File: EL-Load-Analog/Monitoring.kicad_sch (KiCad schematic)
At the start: 65 parts, among them J301 VSense, Q301 2N7002, Q302 BSS138, U301 LM833, U302 LM833, U303 OPA189/MCP6V51/LTC2050HV, U304 OPA189/MCP6V51/LTC2050HV, U305 74HCT02, U306 LM393

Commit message: Major Analog PCB update DAC/ADC + connectors included, fan IC removed
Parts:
- removed J301: VSense, Connector_PinHeader_2.54mm:PinHeader_1x02_P2.54mm_Vertical, symbol Connector:Conn_01x02_Pin
- removed JP301, JP302: Jumper_2_Open, Connector_PinHeader_2.54mm:PinHeader_1x02_P2.54mm_Vertical, symbol Jumper:Jumper_2_Open
- removed JP303, JP304: Jumper_3_Open, Connector_PinHeader_2.54mm:PinHeader_1x03_P2.54mm_Vertical, symbol Jumper:Jumper_3_Open
- removed Q302: BSS138, Package_TO_SOT_SMD:SOT-23, symbol Transistor_FET:BSS138
- removed R326, R327, R328: 10k, Resistor_SMD:R_0805_2012Metric_Pad1.20x1.40mm_HandSolder, symbol Device:R_Small
- removed R329: 20k, Resistor_SMD:R_0805_2012Metric_Pad1.20x1.40mm_HandSolder, symbol Device:R_Small
- added D2, D3: 1N4148, Diode_SMD:D_MiniMELF, symbol Diode:1N4148
- added J6: Conn_02x03_Counter_Clockwise, Connector_PinHeader_2.54mm:PinHeader_2x03_P2.54mm_Vertical_SMD, symbol Connector_Generic:Conn_02x03_Counter_Clockwise
- added K2: EE2-5TNU, Relay_SMD:Relay_DPDT_Kemet_EE2_NU_DoubleCoil, symbol Relay:EE2-5TNU
- added Q1, Q2: 2N7002, Package_TO_SOT_SMD:SOT-23, symbol Transistor_FET:2N7002
- added R1, R16, R18, R19, R20: 100k, Resistor_SMD:R_0805_2012Metric, symbol Device:R_Small
- added U8, U9: VO1400AEFTR, Package_SO:SO-4_4.4x4.3mm_P2.54mm, symbol Relay_SolidState:ASSR-1218
- C1, C2, C301, C302, C303, C304, C305, C306, C307, C308, C309, C310, C311, C312, C313, C314, C315, C316: footprint Capacitor_SMD:C_0805_2012Metric_Pad1.18x1.45mm_HandSolder -> Capacitor_SMD:C_0805_2012Metric
- D301, D302: footprint Diode_SMD:D_MiniMELF_Handsoldering -> Diode_SMD:D_MiniMELF
- JP305: footprint Connector_PinHeader_2.54mm:PinHeader_1x02_P2.54mm_Vertical -> Jumper:SolderJumper-2_P1.3mm_Bridged_RoundedPad1.0x1.5mm
- JP306: footprint Connector_PinHeader_2.54mm:PinHeader_1x02_P2.54mm_Vertical -> Jumper:SolderJumper-2_P1.3mm_Bridged2Bar_RoundedPad1.0x1.5mm
- R301, R302, R303, R304, R305, R306, R307, R308, R309, R310, R311, R312, R313, R314, R315, R316, R317, R318, R319, R320, R321, R322, R323, R324, R325, R330: footprint Resistor_SMD:R_0805_2012Metric_Pad1.20x1.40mm_HandSolder -> Resistor_SMD:R_0805_2012Metric
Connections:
- net -GCOM is gone; now on net GND: U302.5 (+)
- net 4GCOM is gone; now on net GCOM: R315.2
- net +5V: now also D2.1 (K), D3.1 (K), J6.5 (Pin_5), K2.1, K2.6
- net GCOM: now also J6.4 (Pin_4)
- net GND: now also J6.6 (Pin_6), Q1.2 (S), Q2.2 (S), R1.1, R16.1, R20.1, U8.2, U9.2
- net Imon: now also J6.2 (Pin_2)
- net LoadMinMon: now also K2.10
- net LoadPlusMon: now also K2.3
- net LoopImon: now also J6.1 (Pin_1)
- net ~{VonLatch}: now also U305.12
- net ~{Von}: now also Q301.1 (G), U305.4
- net at R312.1, R314.2: now also U9.3
- net at R306.1, R308.2, U303.4 (-): now also U9.4
- net at R316.1, R319.2, U304.4 (-): now also J6.3 (Pin_3)
- net at R305.1, R307.1, U303.3 (+): now also U8.3
- net at R317.2: now also K2.4
- net at R311.2, R313.1: now also U8.4
- net at C310.2, R321.2, U306.3 (+): now also R1.2
- net at R318.1: now also K2.9
- net CCsetOut renamed Iset
- net VonsetComp renamed Vonset
- new net: D3.2 (A), K2.7, Q2.3 (D)
- new net: R19.1, U9.1
- new net: D2.2 (A), K2.12, Q1.3 (D)
- new net: R18.1, U8.1
- new net LoadMinSense: K2.8
- new net LoadPlusSense: K2.5
- new net VoltRangeLow: R18.2, R19.2
- new net VsenseClear: Q2.1 (G), R20.2
- new net VsenseSet: Q1.1 (G), R16.2
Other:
- note added: "For scaling Von"
- note added: "For testing current ranges"
- note added: "Sense selection"
- note added: "TODO: Add protection diodes"
- note added: "TODO: Check this, was -GCOM (-50mV)"
- note added: "Von = VonSet * 34 * 15/16 - 1.6"
- note added: "high(80V)/low(9V) range"
- note removed: "Manual high(80V)/low(9V) range"
- note removed: "Manual sense selection"
- moved on the sheet: C307, C308, R321

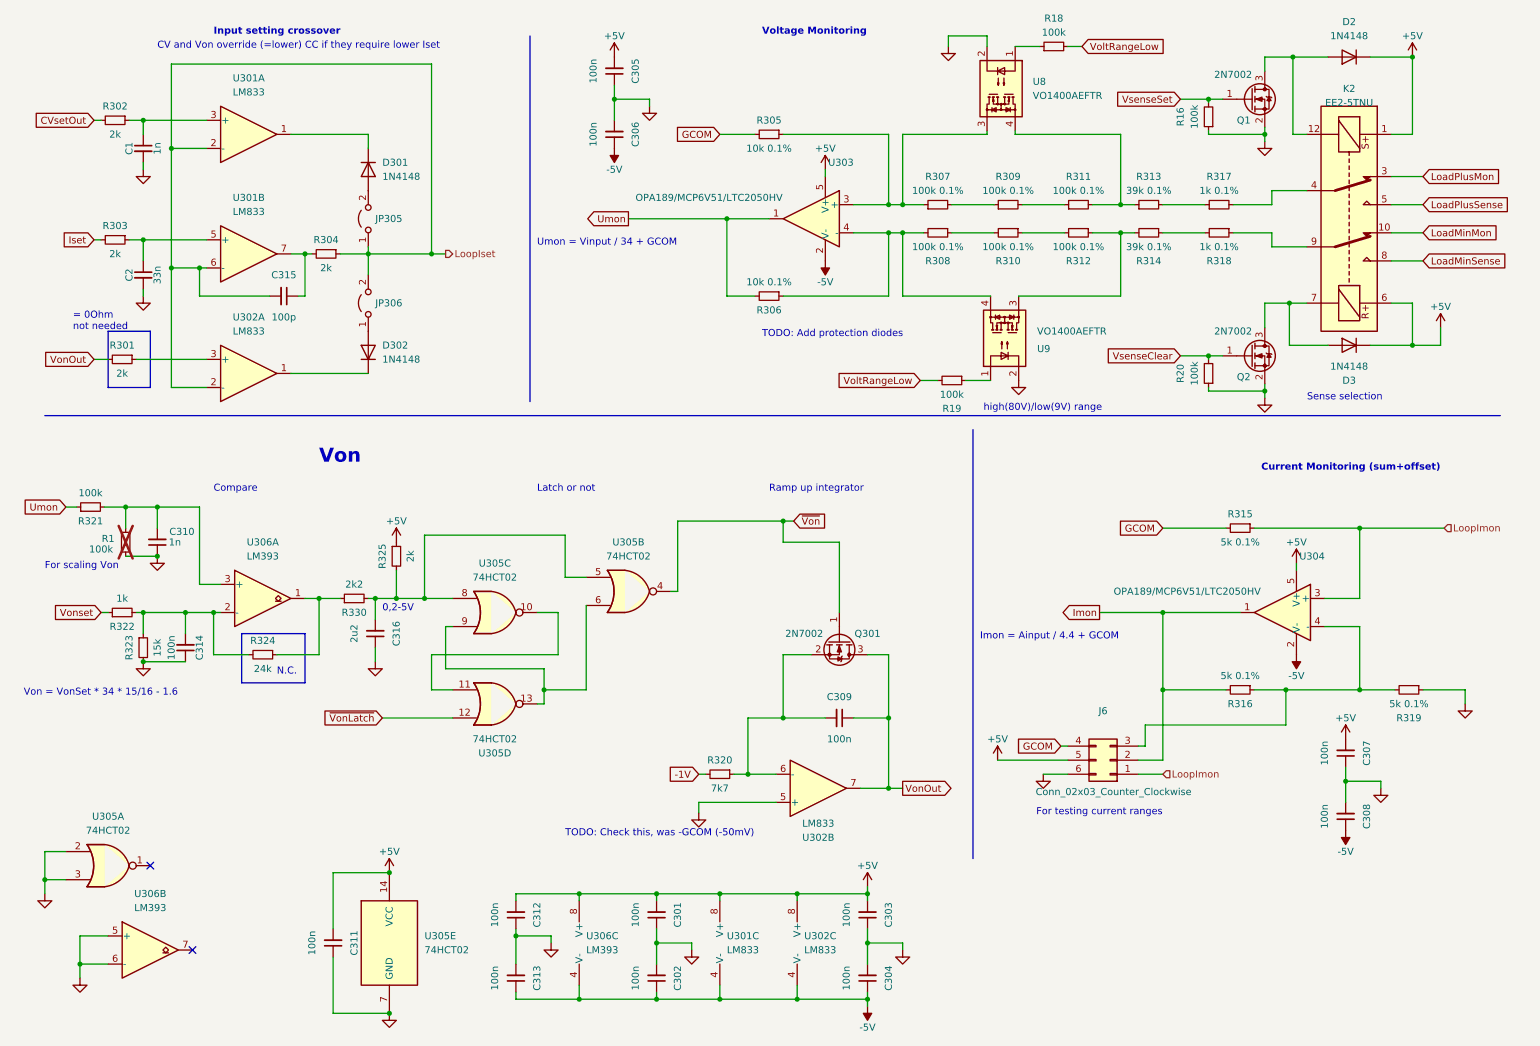
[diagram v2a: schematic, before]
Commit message: Added SenseError detection (including ocmponents), added clearances, fixed few BOM items.
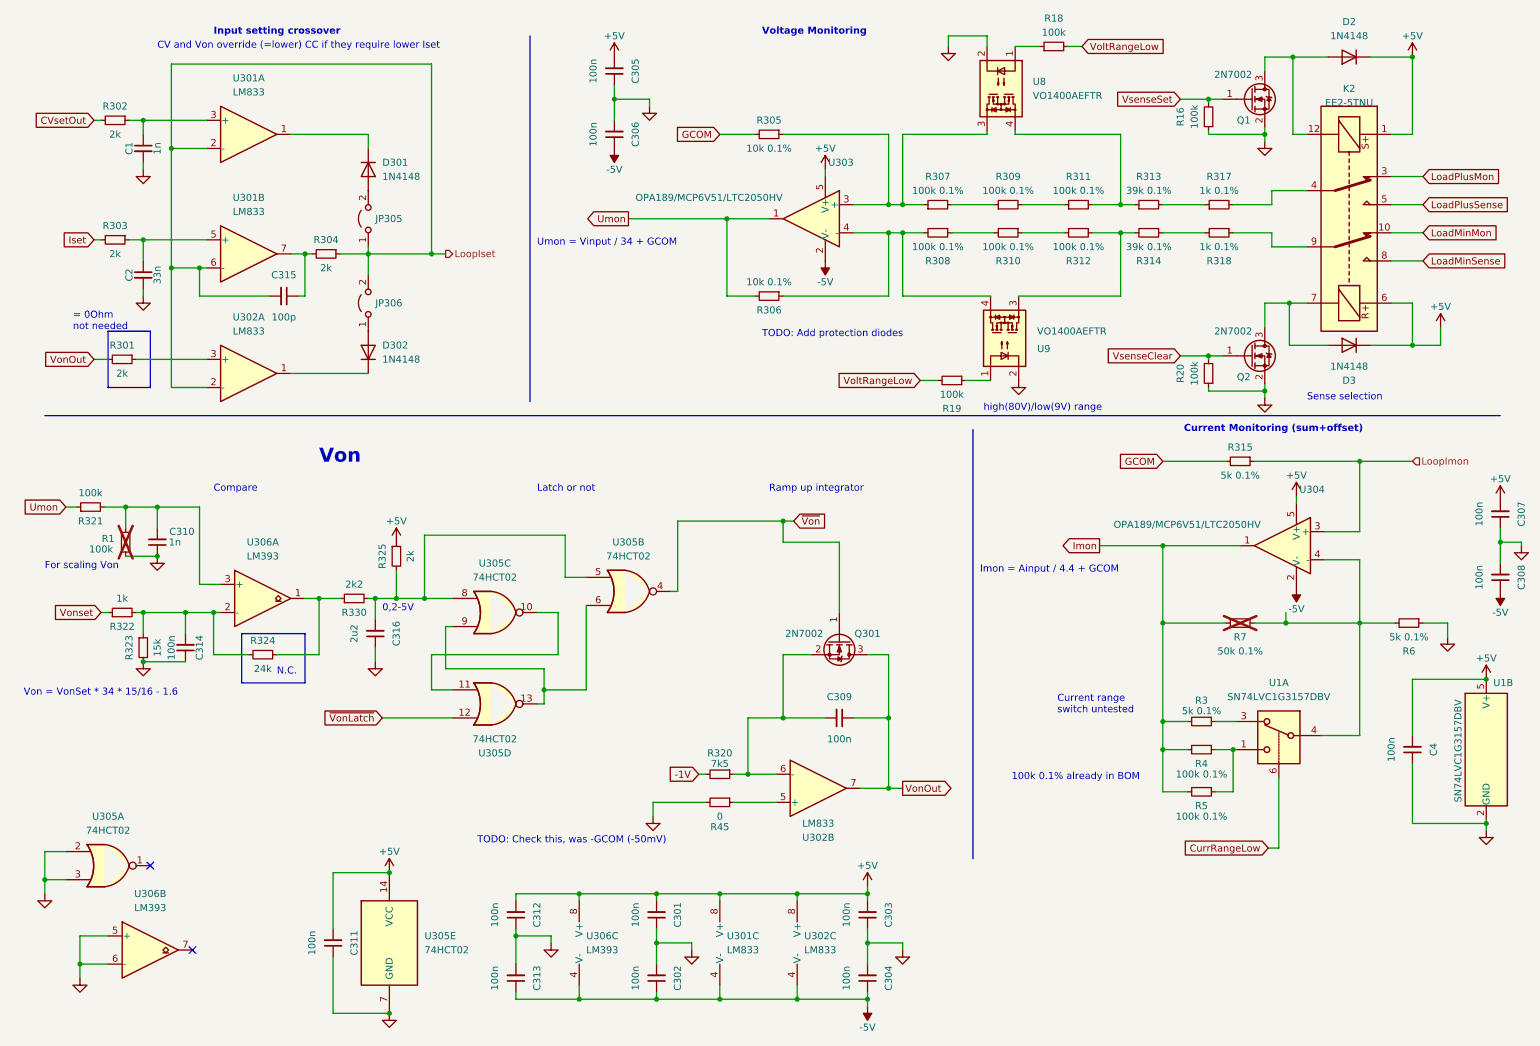
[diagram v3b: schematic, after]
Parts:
- removed J6: Conn_02x03_Counter_Clockwise, Connector_PinHeader_2.54mm:PinHeader_2x03_P2.54mm_Vertical_SMD, symbol Connector_Generic:Conn_02x03_Counter_Clockwise
- added C4: 100n, Capacitor_SMD:C_0805_2012Metric, symbol Device:C_Small
- added R3: 5k 0.1%, Resistor_SMD:R_0805_2012Metric, symbol Device:R_Small
- added R4, R5: 100k 0.1%, Resistor_SMD:R_0805_2012Metric, symbol Device:R_Small
- added R45: 0, Resistor_SMD:R_0805_2012Metric, symbol Device:R_Small
- added U1: SN74LVC1G3157DBV, Package_TO_SOT_SMD:SOT-23-6, symbol Analog_Switch:TS5A63157DBV
- C1, C310: Part Name (none) -> C_1.0nF_0805_20%
- C2: Part Name (none) -> C_33.0nF_0805_20%
- C301, C302, C303, C304, C305, C306, C307, C308, C309, C311, C312, C313, C314: Part Name (none) -> C_100.0nF_0805_20%
- C315: Part Name (none) -> C_100.0pF_0805_20%
- C316: Part Name (none) -> C_2.2uF_10V_X7R_10%_0805
- D2, D3, D301, D302: Part Name (none) -> D_1N4148_miniMELF
- K2: Part Name (none) -> ER_EE2-5TNU-L
- Q1, Q2, Q301: Part Name (none) -> Q_2N7002
- R1, R16, R18, R19, R20, R321: Part Name (none) -> R_100.0kΩ_0805_1%
- R301, R302, R303, R304, R325: Part Name (none) -> R_2.0kΩ_0805_1%
- R305, R306: Part Name (none) -> R_10k_0805_0.1%
- R307, R308, R309, R310, R311, R312: Part Name (none) -> R_100k_0805_0.1%
- R313, R314: Part Name (none) -> R_39k_0805_0.1%
- R315: Part Name (none) -> R_5k_0805_0.1%
- R317, R318: Part Name (none) -> R_1k_0805_0.1%
- R320: value 7k7 -> 7k5; Part Name (none) -> R_7.5kΩ_0805_1%
- R322: Part Name (none) -> R_1.0kΩ_0805_1%
- R323: Part Name (none) -> R_15.0kΩ_0805_1%
- R324: Part Name (none) -> R_24.0kΩ_0805_1%
- R330: Part Name (none) -> R_2.2kΩ_0805_1%
- R6: renamed from R319; Part Name (none) -> R_5k_0805_0.1%
- R7: renamed from R316; value 5k 0.1% -> 50k 0.1%; now not fitted; now left out of the parts list
- U301, U302: Part Name (none) -> U_LM833DR
- U303, U304: Part Name (none) -> U_LTC2050HVCS5
- U305: Part Name (none) -> U_74HCT02D
- U306: Part Name (none) -> U_LM393
- U8, U9: Part Name (none) -> U_VO1400AEFTR
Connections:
- net +5V: now also C4.2, U1.5 (V+)
- net GND: now also C4.1, R45.2, U1.2 (GND); no longer U302.5 (+)
- net Imon: now also R3.2, R4.2, R5.2
- net at R6.2, R7.1, U304.4 (-): now also U1.4
- new net: R4.1, R5.1, U1.1
- new net: R45.1, U302.5 (+)
- new net: R3.1, U1.3
- new net CurrRangeLow: U1.6
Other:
- note added: "100k 0.1% already in BOM"
- note added: "Current range switch untested"
- note removed: "For testing current ranges"
- moved on the sheet: C307, C308, R315, R6, U304
